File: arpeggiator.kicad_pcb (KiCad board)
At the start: 2 copper layers, 220 x 170 mm, 360 parts, among them J202 logic test header, J601 3.5mm mono line out, J701 PJ-102AH / 12V DC centre +, Q601 2N7002, Q602 MMBT3904, Q603 BSS84, Q604 MMBT3904, Q605 2N7002, Q606 MMBT3906, Q701 AO3401A, Q702 MMBT3906, Q703 MMBT3906, SW101 C, SW102 C sharp, SW103 D, SW104 D sharp, SW105 E, SW106 F, SW107 F sharp, SW108 G, SW109 G sharp, SW110 A, SW111 A sharp, SW112 B, SW113 start / stop, SW114 1 / 2 / 3 octaves, SW601 saw / pulse, U101 TLC555IDR, U102 TLC555IDR, U103 MCP100T-450I/TT, U201 74HC574, U202 74HC574, U203 74HC574, U204 74HC574, U205 74HC377, U206 74HC377, U211 74HC163, U212 74HC138, U213 74HC163, U214 74HC163, U215 74HC163, U216 CD74HC4067M, U221 74HC377, U222 74HC154, U301 74HC74, U302 74HC74, U303 74HC74, U401 74HC14, U402 74HC14, U403 74HC14, U404 74HC04, U405 74HC04, U406 74HC08, U407 74HC86, U408 74HC04, U409 74HC32, U410 74HC32, U411 74HC32, U412 74HC32, U413 74HC08, U414 74HC08, U415 74HC86, U416 74HC04, U417 74HC08, U418 74HC08, U419 74HC32, U420 74HC14, U421 74HC08, U422 74HC32, U423 74HC08, U424 74HC32, U425 74HC08, U501 OPA4192IDR, U502 ADG706BRUZ, U503 74HC4051D, U504 AS3340A, U601 TLC555IDR, U602 OPA4192IDR, U603 TL074HIDR, U604 LM13700M/NOPB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

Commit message: start routing the board
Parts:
- moved C716 133.9 mm to (208.2, 112.2), turned to 180 degrees
- moved D705 127.9 mm to (213.0, 108.5), turned to 0 degrees
- moved U705 125.1 mm to (203.0, 112.0)
- moved D706 123.9 mm to (197.5, 113.0)
- moved C715 123.2 mm to (200.8, 108.0), turned to 90 degrees
- moved R636 119.4 mm to (216.0, 111.5)
- moved C944 102.3 mm to (101.8, 141.2), turned to -90 degrees
- moved R624 97.5 mm to (182.0, 127.5)
- moved R623 96.6 mm to (179.0, 126.5), turned to 90 degrees
- moved C934 94.0 mm to (42.8, 132.0), turned to -90 degrees
- moved C918 92.8 mm to (58.8, 133.8), turned to -90 degrees
- moved C935 92.0 mm to (34.5, 130.0), turned to -90 degrees
- moved C556 88.6 mm to (189.8, 121.0), turned to 180 degrees
- moved R141 88.0 mm to (199.0, 86.5)
- moved C937 88.0 mm to (85.5, 126.0), turned to -90 degrees
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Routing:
- net +5V: track 0.00 -> 1538.2 mm, vias 0 -> 26
- net +12V: track 0.00 -> 384.0 mm, vias 0 -> 14
- net RESET_N: track 0.00 -> 381.1 mm, vias 0 -> 25
- net FAST_CLK: track 0.00 -> 367.3 mm, vias 0 -> 19
- net -5V: track 0.00 -> 358.0 mm, vias 0 -> 8
- net AUDIO_ENABLE: track 0.00 -> 259.3 mm, vias 0 -> 7
- net REF2V5: track 0.00 -> 238.4 mm, vias 0 -> 3
- net N2: track 0.00 -> 182.8 mm, vias 0 -> 13
- net N0: track 0.00 -> 178.8 mm, vias 0 -> 17
- net Net-(C631-Pad2): track 0.00 -> 178.4 mm, vias 0 -> 1
- net RUN: track 0.00 -> 165.6 mm, vias 0 -> 11
- net O0: track 0.00 -> 160.0 mm, vias 0 -> 11
- net RANGE1: track 0.00 -> 156.7 mm, vias 0 -> 17
- net Net-(C632-Pad2): track 0.00 -> 150.4 mm, vias 0 -> 2
- net FINE_W: track 0.00 -> 139.7 mm, vias 0 -> 1
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- added copper zone on B.Cu, net GND
- added copper zone on F.Cu, net GND

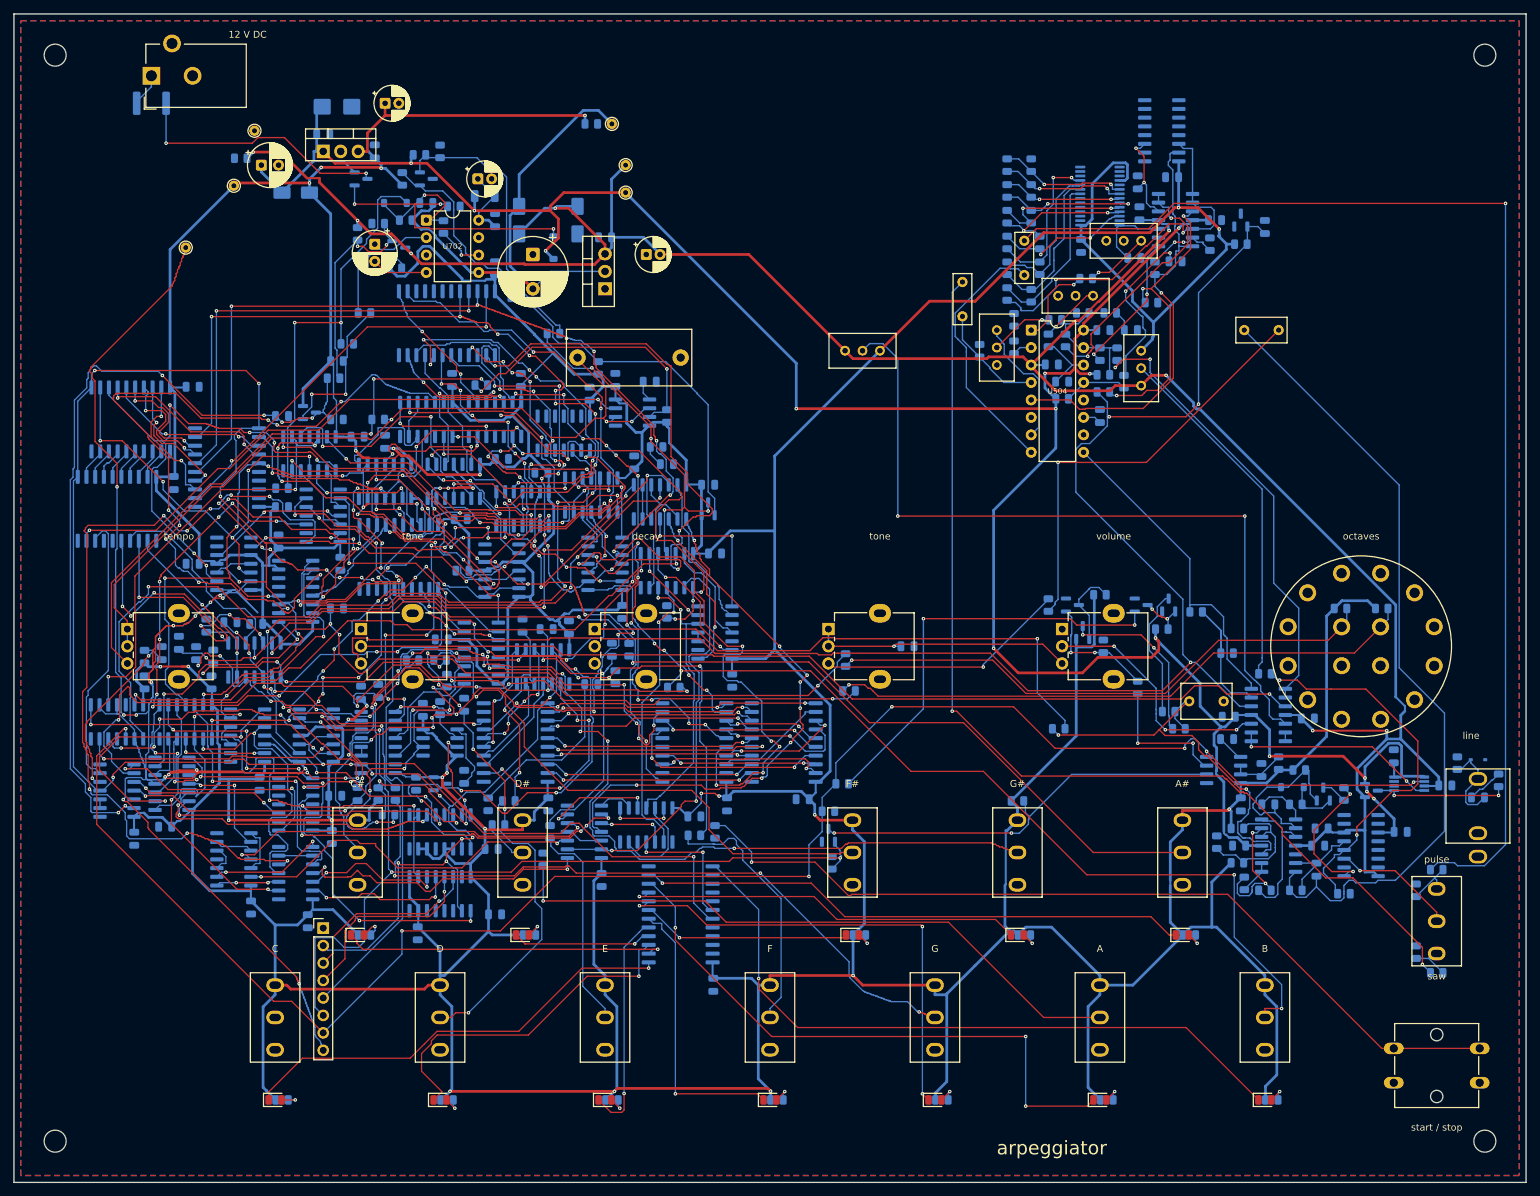
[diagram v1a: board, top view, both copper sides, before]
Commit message: clean up routing and connect more ground returns
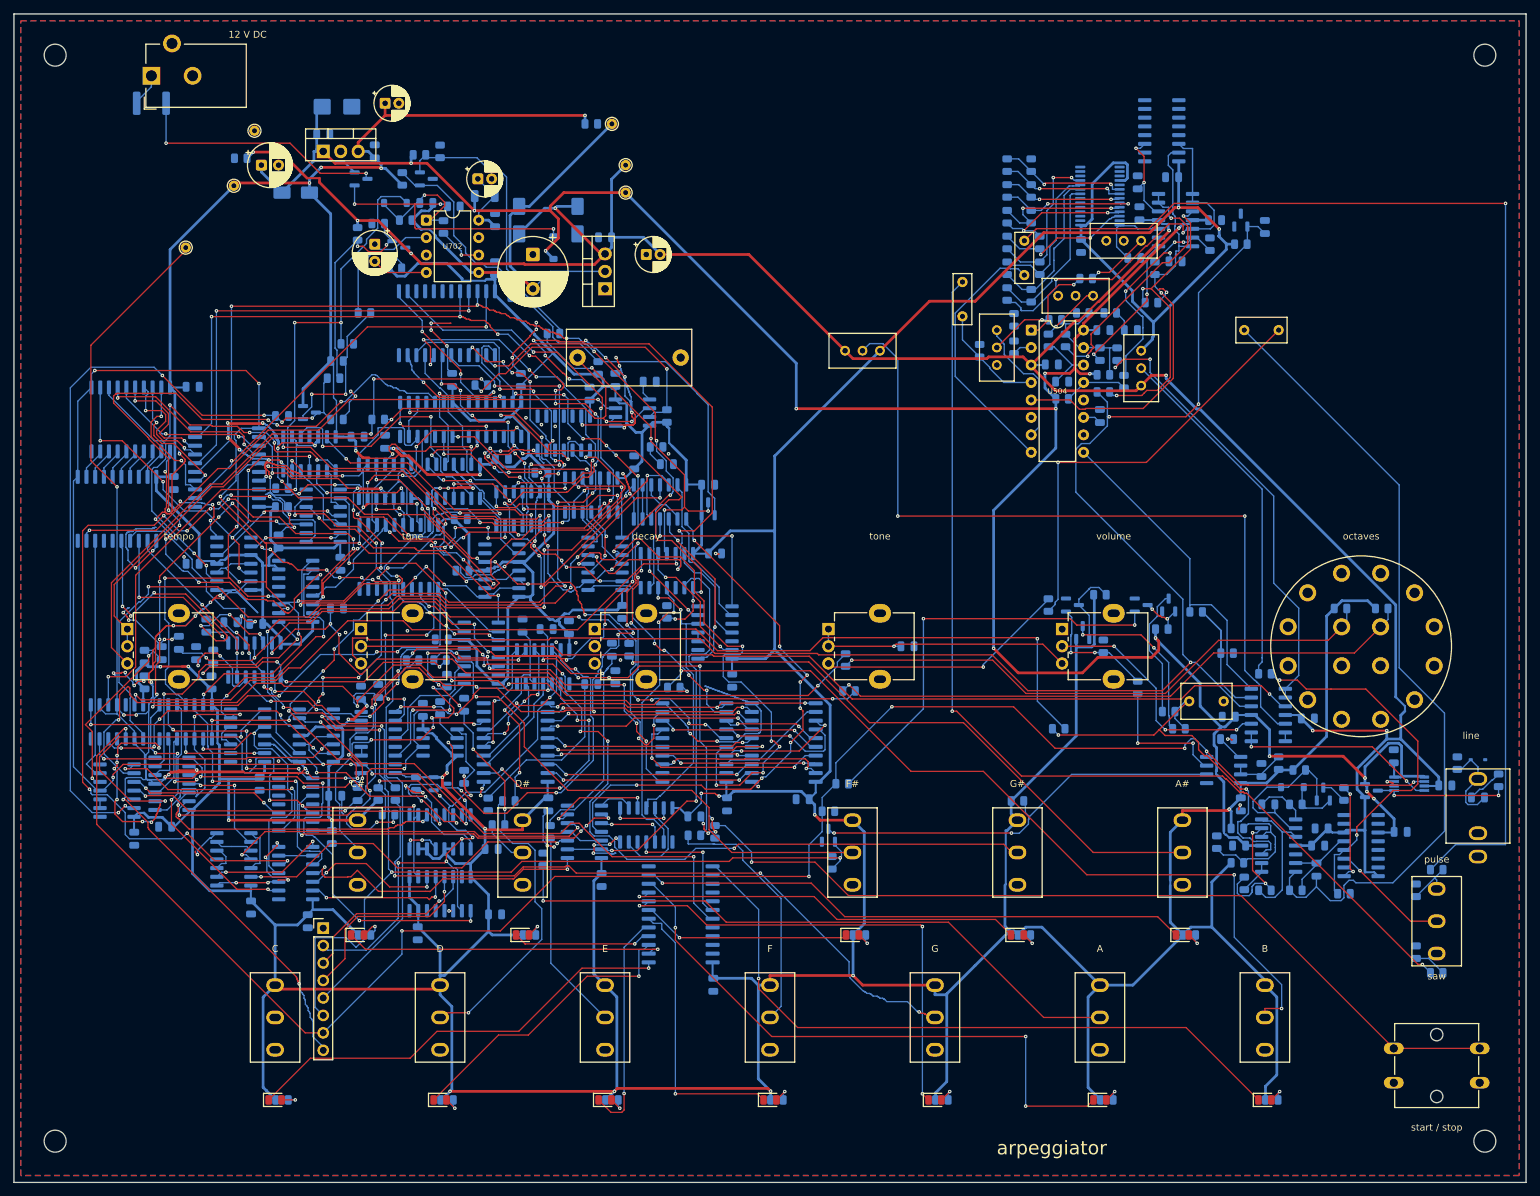
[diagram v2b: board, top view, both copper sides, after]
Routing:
- net GND: track 0.00 -> 402.1 mm, vias 0 -> 110
- net LED_N2: track 50.6 -> 42.9 mm
- net +5V: track 1538.2 -> 1531.4 mm
- net I_ABC: track 20.5 -> 14.3 mm
- net VNEG_RAW: track 74.6 -> 70.3 mm
- net G066: track 43.0 -> 39.0 mm
- net BUTTON_IN: track 40.2 -> 36.3 mm
- net TIM161: track 115.6 -> 113.2 mm
- net Net-(C632-Pad2): track 150.4 -> 148.5 mm
- net SW_N6: track 81.6 -> 80.0 mm
- net NOTE_SNAP7: track 85.2 -> 83.7 mm
- net SW_N4: track 30.7 -> 29.4 mm
- net OTA_ZERO: track 56.4 -> 55.1 mm
- net NOTE_IN10: track 29.9 -> 28.7 mm
- net FAST_CLK: track 367.3 -> 366.3 mm
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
